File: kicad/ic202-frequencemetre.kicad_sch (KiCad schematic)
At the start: 40 parts, among them J1 +12V IN, J2 RF IN, J4 LCD, Q1 2N2369, U1 L7805, U2 LM317L, U3 MB506

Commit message: Documente l'intention de conception via la propriete Placement
Applique le skill conception-electronique-kicad au schema existant :
propriete masquee Placement posee sur chaque composant dont la position
finale importe au-dela du raccordement electrique.

Decouplage documente (prefixe LOCAL) : C1/C2 (entree J1, IN de U1), C3/C4
(noeud partage OUT U1 / VI U2), C5/C6 (sortie U2), C9 (VCC de U3), C8 (~IN
de U3, decouplage HF sur broche signal - pas une broche d'alimentation),
C11 (rail +3V pres de R6, point le plus eloigne du regulateur), C12
(reference VLCD_MID).

Verification systematique menee : les trois CI actifs (U1, U2, U3) ont
chacun leur decouplage local documente. A1 (module Arduino complet, deja
decouple en interne) volontairement hors de cette verification.

Boucles critiques documentees (prefixe LOOP CRITIQUE, hors decouplage) :
J2-R3-C7 (chemin RF d'entree vers U3, jusqu'a 2,4GHz), et
U3(OUT)-R19-C10-R4-R6-Q1 (chemin de comptage vers D5_SIG de A1, le signal
que l'instrument mesure).

Aucun changement electrique ni visuel : proprietes masquees par defaut,
netlist identique (40 composants, 22 nets), rendu confirme inchange. ERC :
0 erreur, 0 avertissement. Regles de lisibilite verifiees.

Co-Authored-By: Claude Sonnet 5 <noreply@anthropic.com>
Claude-Session: https://claude.ai/code/session_017jkpXZgM5sH1vt8JFfAijf
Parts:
- C1: Placement (none) -> LOCAL - decouplage HF, coller pres de l'entree J1 et de la 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
- C10: Placement (none) -> LOOP CRITIQUE - pas du decouplage : couplage AC + chemin de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
- C11: Placement (none) -> LOCAL - decouplage HF du rail +3V pres de R6 (tirage collec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
- C12: Placement (none) -> LOCAL - decouplage de la reference VLCD_MID, coller au poin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
- C2: Placement (none) -> LOCAL - decouplage bulk BF, coller pres de l'entree J1 et d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
- C3: Placement (none) -> LOCAL - decouplage HF, coller au noeud +5V (broche 3 OUT de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
- C4: Placement (none) -> LOCAL - decouplage bulk BF, coller au noeud +5V (broche 3 O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
- C5: Placement (none) -> LOCAL - decouplage HF, coller broche 2 (VO, sortie) de U2
- C6: Placement (none) -> LOCAL - decouplage bulk BF, coller broche 2 (VO, sortie) de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
- C7: Placement (none) -> LOOP CRITIQUE - pas du decouplage : couplage AC + chemin RF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
- C8: Placement (none) -> LOCAL - decouplage HF de la broche 8 (~IN, entree complemen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
- C9: Placement (none) -> LOCAL - decouplage HF, coller broche 2 (VCC) de U3
- J2, R3: Placement (none) -> LOOP CRITIQUE - chemin RF d'entree J2-R3-C7 vers U3 (broche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
- Q1, R4, R6: Placement (none) -> LOOP CRITIQUE - chemin de comptage U3(OUT)-R19-C10-R4-R6-Q1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
- R19: Placement (none) -> LOOP CRITIQUE - pas du decouplage : terminaison + chemin de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
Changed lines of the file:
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@@
 			)
 		)
+    (property "Placement" "LOCAL - decouplage HF, coller pres de l'entree J1 et de la broche 1 (IN) de U1" (at 48.26 38.1 0)
+      (effects (font (size 1.27 1.27)) (hide yes))
+    )
 		(pin "1"
 		)
@@
 			)
 		)
+    (property "Placement" "LOCAL - decouplage HF, coller au noeud +5V (broche 3 OUT de U1 / broche 3 VI de U2)" (at 104.14 38.1 0)
+      (effects (font (size 1.27 1.27)) (hide yes))
+    )
 		(pin "1"
 		)
@@
 			)
 		)
+    (property "Placement" "LOCAL - decouplage bulk BF, coller pres de l'entree J1 et de la broche 1 (IN) de U1" (at 58.42 38.1 0)
+      (effects (font (size 1.27 1.27)) (hide yes))
+    )
 		(pin "1"
 		)
@@
 			)
 		)
+    (property "Placement" "LOCAL - decouplage de la reference VLCD_MID, coller au point milieu du pont R17/R18" (at 309.88 220.98 0)
+      (effects (font (size 1.27 1.27)) (hide yes))
+    )
 		(pin "1"
 		)
@@
 			)
 		)
+    (property "Placement" "LOCAL - decouplage HF de la broche 8 (~IN, entree complementaire) de U3 vers la masse, pas du decouplage d'alimentation - coller a la broche avec R20" (at 55.88 114.3 0)
+      (effects (font (size 1.27 1.27)) (hide yes))
+    )
 		(pin "1"
 		)
@@
 			)
 		)
+    (property "Placement" "LOOP CRITIQUE - chemin de comptage U3(OUT)-R19-C10-R4-R6-Q1 vers D5_SIG (broche 8 de A1), surface minimale, eloigner des sources de bruit" (at 142.24 95.25 0)
+      (effects (font (size 1.27 1.27)) (hide yes))
+    )
 		(pin "1"
 		)
@@
 			)
 		)
+    (property "Placement" "LOOP CRITIQUE - pas du decouplage : terminaison + chemin de comptage U3(OUT)-R19-C10-R4-R6-Q1 vers D5_SIG (broche 8 de A1), surface minimale, eloigner des sources de bruit" (at 107.95 109.22 0)
+      (effects (font (size 1.27 1.27)) (hide yes))
+    )
 		(pin "1"
 		)
@@
 			)
 		)
+    (property "Placement" "LOCAL - decouplage HF du rail +3V pres de R6 (tirage collecteur Q1), point le plus eloigne du regulateur U2" (at 280.67 102.87 0)
+      (effects (font (size 1.27 1.27)) (hide yes))
+    )
 		(pin "1"
 		)
@@
 			)
 		)
+    (property "Placement" "LOCAL - decouplage bulk BF, coller au noeud +5V (broche 3 OUT de U1 / broche 3 VI de U2)" (at 114.3 38.1 0)
+      (effects (font (size 1.27 1.27)) (hide yes))
+    )
 		(pin "1"
 		)
@@
 			)
 		)
+    (property "Placement" "LOCAL - decouplage bulk BF, coller broche 2 (VO, sortie) de U2" (at 193.04 38.1 0)
+      (effects (font (size 1.27 1.27)) (hide yes))
+    )
 		(pin "1"
 		)
@@
 			)
 		)
+    (property "Placement" "LOOP CRITIQUE - pas du decouplage : couplage AC + chemin RF d'entree J2-R3-C7 vers U3 (broche 1, IN), surface minimale imperative (signal jusqu'a 2,4GHz)" (at 60.96 101.6 0)
+      (effects (font (size 1.27 1.27)) (hide yes))
+    )
 		(pin "1"
 		)
@@
 			)
 		)
+    (property "Placement" "LOOP CRITIQUE - chemin de comptage U3(OUT)-R19-C10-R4-R6-Q1 vers D5_SIG (broche 8 de A1), surface minimale, eloigner des sources de bruit" (at 162.56 86.36 0)
+      (effects (font (size 1.27 1.27)) (hide yes))
+    )
 		(pin "1"
 		)
@@
 			)
 		)
+    (property "Placement" "LOOP CRITIQUE - chemin de comptage U3(OUT)-R19-C10-R4-R6-Q1 vers D5_SIG (broche 8 de A1), surface minimale, eloigner des sources de bruit" (at 160.02 101.6 0)
+      (effects (font (size 1.27 1.27)) (hide yes))
+    )
 		(pin "1"
 		)
@@
 			)
 		)
+    (property "Placement" "LOOP CRITIQUE - pas du decouplage : couplage AC + chemin de comptage U3(OUT)-R19-C10-R4-R6-Q1 vers D5_SIG (broche 8 de A1), surface minimale, eloigner des sources de bruit" (at 119.38 101.6 0)
+      (effects (font (size 1.27 1.27)) (hide yes))
+    )
 		(pin "1"
 		)
@@
 			)
 		)
+    (property "Placement" "LOCAL - decouplage HF, coller broche 2 (VO, sortie) de U2" (at 182.88 38.1 0)
+      (effects (font (size 1.27 1.27)) (hide yes))
+    )
 		(pin "1"
 		)
@@
 			)
 		)
+    (property "Placement" "LOOP CRITIQUE - chemin RF d'entree J2-R3-C7 vers U3 (broche 1, IN), surface minimale imperative (signal jusqu'a 2,4GHz)" (at 43.18 109.22 0)
+      (effects (font (size 1.27 1.27)) (hide yes))
+    )
 		(pin "1"
 		)
@@
 			)
 		)
+    (property "Placement" "LOCAL - decouplage HF, coller broche 2 (VCC) de U3" (at 104.14 127.0 0)
+      (effects (font (size 1.27 1.27)) (hide yes))
+    )
 		(pin "1"
 		)
@@
 			)
 		)
-		(pin "1"
-		)
+    (property "Placement" "LOOP CRITIQUE - chemin RF d'entree J2-R3-C7 vers U3 (broche 1, IN), surface minimale imperative (signal jusqu'a 2,4GHz)" (at 30.48 101.6 0)
+      (effects (font (size 1.27 1.27)) (hide yes))
+    )
+		(pin "1"
+		)

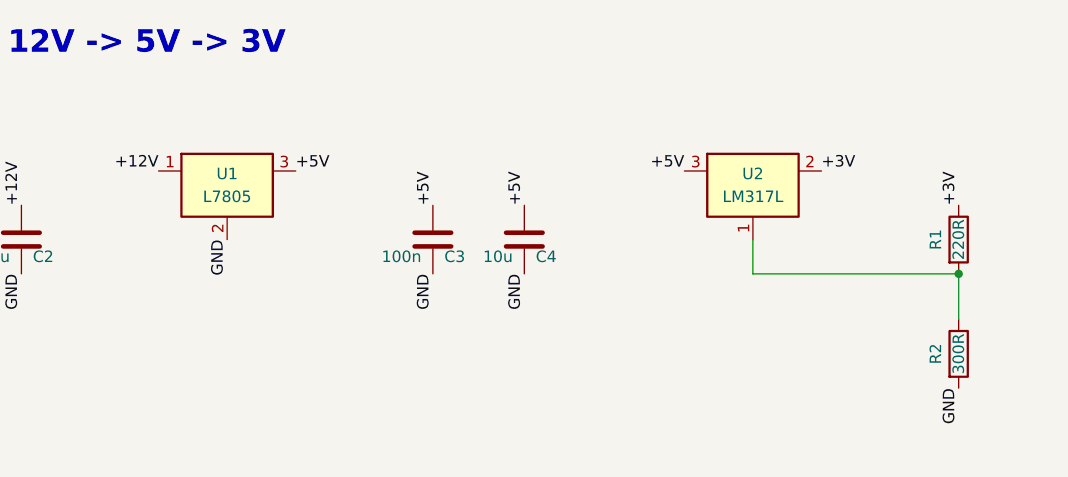
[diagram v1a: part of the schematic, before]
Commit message: Regulateurs en CMS : L7805->AMS1117-5.0, LM317L->AMS1117 ajustable
Stock PartsBox de l'utilisateur consulte avant de figer le choix (suivant
le skill conception-electronique-kicad) : ni L7805 ni LM317L en CMS en
stock, mais AMS1117-5.0 (68), AMS1117 ajustable (10) et AMS1117-3.3 (71)
en SOT-223, tous chez le meme fournisseur de stockage (C3 small
regulators). Choix retenu par l'utilisateur : AMS1117-5.0 pour U1,
AMS1117 ajustable pour U2 - topologie inchangee (meme reference 1,25V que
le LM317, R1/R2 conserves a l'identique).

Geometrie de broches verifiee avant remplacement : AMS1117-5.0 et L7805
partagent les memes coordonnees de broches (seule la numerotation change :
IN/OUT deviennent VI=broche3/VO=broche2), AMS1117 ajustable et LM317L_TO92
partagent numerotation ET coordonnees a l'identique. replace_schematic_
component utilise pour preserver position/rotation ; connectivite
reverifiee par export netlist apres coup - correcte des le premier essai.

Empreinte SOT-223-3_TabPin2 pour les deux (tab electriquement relie a VO,
conforme au brochage reel de l'AMS1117), rechargement pcbnew confirme.

Proprietes Placement de C1-C4 mises a jour pour refleter la nouvelle
numerotation des broches de U1. README revu integralement (alimentation,
mise en forme, tableau d'hypotheses, tableau de decouplage).

ERC : 0 erreur, 0 avertissement. Netlist identique (40 composants, 22
nets). Regles de lisibilite verifiees.

Co-Authored-By: Claude Sonnet 5 <noreply@anthropic.com>
Claude-Session: https://claude.ai/code/session_017jkpXZgM5sH1vt8JFfAijf
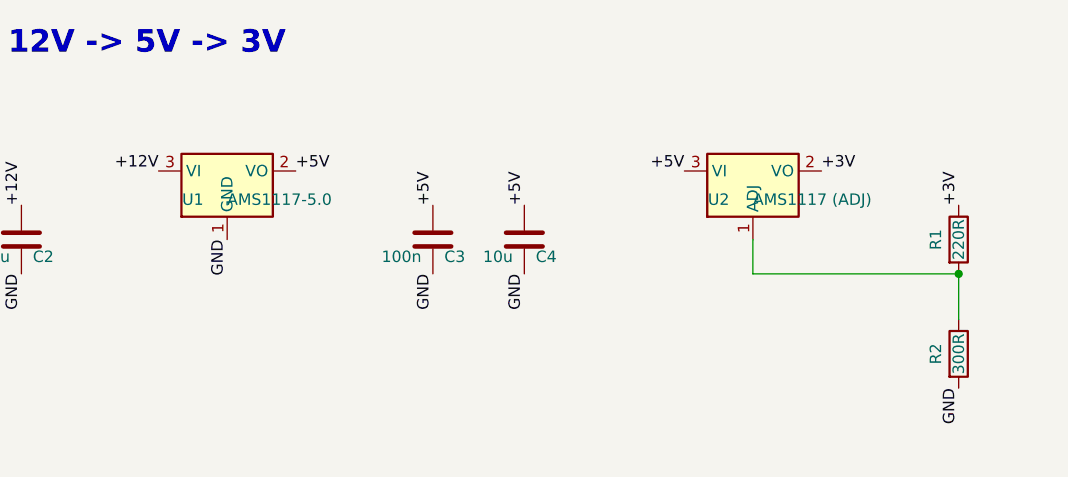
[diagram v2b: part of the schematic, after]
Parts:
- removed U1: L7805, Package_TO_SOT_THT:TO-220-3_Vertical, symbol Regulator_Linear:L7805
- removed U2: LM317L, Package_TO_SOT_THT:TO-92_Inline, symbol Regulator_Linear:LM317L_TO92
- added U1: AMS1117-5.0, Package_TO_SOT_SMD:SOT-223-3_TabPin2, symbol Regulator_Linear:AMS1117-5.0
- added U2: AMS1117 (ADJ), Package_TO_SOT_SMD:SOT-223-3_TabPin2, symbol Regulator_Linear:AMS1117
- C1: Placement LOCAL - decouplage HF, coller pres de l'entree J1 et de la broche 1 (IN) de U1 -> LOCAL - decouplage HF, coller pres de l'entree J1 et de la broche 3 (VI) de U1
- C2: Placement LOCAL - decouplage bulk BF, coller pres de l'entree J1 et de la broche 1 (IN) de U1 -> LOCAL - decouplage bulk BF, coller pres de l'entree J1 et de la broche 3 (VI) de U1
- C3: Placement LOCAL - decouplage HF, coller au noeud +5V (broche 3 OUT de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 -> LOCAL - decouplage HF, coller au noeud +5V (broche 2 VO de 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
- C4: Placement LOCAL - decouplage bulk BF, coller au noeud +5V (broche 3 O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 -> LOCAL - decouplage bulk BF, coller au noeud +5V (broche 2 V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
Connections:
- net +12V: now also U1.3 (VI)
- net +3V: now also U2.2 (VO)
- net +5V: now also U1.2 (VO), U2.3 (VI)
- net GND: now also U1.1 (GND)
- net at R1.2, R2.1: now also U2.1 (ADJ)

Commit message: U3->SOP-8, Q1->SOT-89, J1->4 broches ; cavaliers devant J4 ; replacement 80x50mm
Schema :
- U3 (MB506) : DIP-8 -> SOP-8 (MB506PF Fujitsu, stock PartsBox), meme
  brochage 1-8, pas de changement de symbole.
- Q1 : 2N2369 (TO-18) -> 2SC5551AE-TD-E (onsemi, SOT-89, fT=3.5GHz, stock
  PartsBox). Symbole remplace par Q_NPN_BCE (meme geometrie de broches que
  Q_NPN_BEC, seul l'etiquetage broche/fonction change) pour correspondre au
  brochage reel du SOT-89 (broche 2 = collecteur sur la languette).
- J1 : connecteur 2 broches -> 4 broches, paires adjacentes 1-2=+12V et
  3-4=GND. Corrige au passage un bug preexistant (les 2 broches d'origine
  et leurs labels +12V/GND etaient orphelins, non relies par un fil).
- 10 cavaliers a souder JP1-JP10 (Jumper:SolderJumper_2_Open, ouverts par
  defaut) inseres en serie entre R7-R16 et chaque broche de J4, pour
  pouvoir isoler la carte de la nappe LCD.

PCB :
- Board reduit de 80x70mm a 80x50mm.
- Nouveau placement complet : A1 decale de 3mm vers la gauche, R7-R16
  places dans le volume libre sous A1 (entre les deux barrettes de picots),
  reste reparti par proximite. 0 erreur run_drc (kicad-cli), 3
  avertissements silkscreen cosmetiques.
- Limitation d'outil documentee (README + skill kicad-pcb-placement) :
  check_courtyard_overlaps (MCP) juge sur la bounding box globale d'une
  empreinte, pas ses polygones reels - faux positifs sur les empreintes a
  courtyards multiples comme celle de A1. run_drc fait foi.

Co-Authored-By: Claude Sonnet 5 <noreply@anthropic.com>
Claude-Session: https://claude.ai/code/session_017jkpXZgM5sH1vt8JFfAijf
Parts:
- removed J1: +12V IN, Connector_PinHeader_2.54mm:PinHeader_1x02_P2.54mm_Vertical, symbol Connector_Generic:Conn_01x02
- removed Q1: 2N2369, Package_TO_SOT_THT:TO-92_Inline, symbol Transistor_BJT:Q_NPN_BEC
- added J1: +12V IN (4 pins: 2x+12V, 2x GND), Connector_PinHeader_2.54mm:PinHeader_1x04_P2.54mm_Vertical, symbol Connector_Generic:Conn_01x04
- added JP1, JP10, JP2, JP3, JP4, JP5, JP6, JP7, JP8, JP9: SolderJumper_2_Open, Jumper:SolderJumper-2_P1.3mm_Open_Pad1.0x1.5mm, symbol Jumper:SolderJumper_2_Open
- added Q1: 2SC5551AE-TD-E, Package_TO_SOT_SMD:SOT-89-3, symbol Transistor_BJT:Q_NPN_BCE
- U3: footprint Package_DIP:DIP-8_W7.62mm -> Package_SO:SOIC-8_5.3x6.2mm_P1.27mm
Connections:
- net +12V: now also J1.1 (Pin_1), J1.2 (Pin_2)
- net D5_SIG: now also Q1.2 (C)
- net GND: now also J1.3 (Pin_3), J1.4 (Pin_4), Q1.3 (E)
- net LCD_COM1: now also JP1.1 (A); no longer J4.1 (Pin_1)
- net LCD_COM2: now also JP2.1 (A); no longer J4.2 (Pin_2)
- net LCD_COM3: now also JP3.1 (A); no longer J4.3 (Pin_3)
- net LCD_COM4: now also JP4.1 (A); no longer J4.4 (Pin_4)
- net LCD_SEG1: now also JP5.1 (A); no longer J4.5 (Pin_5)
- net LCD_SEG2: now also JP6.1 (A); no longer J4.6 (Pin_6)
- net LCD_SEG3: now also JP7.1 (A); no longer J4.7 (Pin_7)
- net LCD_SEG4: now also JP8.1 (A); no longer J4.8 (Pin_8)
- net LCD_SEG5: now also JP9.1 (A); no longer J4.9 (Pin_9)
- net LCD_SEG6: now also JP10.1 (A); no longer J4.10 (Pin_10)
- net at C10.2, R4.1: now also Q1.1 (B)
- new net: J4.10 (Pin_10), J4.7 (Pin_7), J4.8 (Pin_8), J4.9 (Pin_9), JP10.2 (B), JP7.2 (B), JP8.2 (B), JP9.2 (B)
- new net: J4.1 (Pin_1), J4.2 (Pin_2), J4.3 (Pin_3), J4.4 (Pin_4), J4.5 (Pin_5), JP1.2 (B), JP2.2 (B), JP3.2 (B), JP4.2 (B), JP5.2 (B)
- new net: J4.6 (Pin_6), JP6.2 (B)

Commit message: Corrige un court-circuit entre lignes LCD introduit par le routage des cavaliers
Les 10 fils cavalier->J4 passaient par un coude a abscisse commune
(x=330.2). Les pas differents cote resistances (5,08mm) et cote J4
(2,54mm) faisaient que plusieurs segments verticaux se chevauchaient sur
cette abscisse, court-circuitant COM2-COM3-COM4-SEG1 d'un cote et
SEG3-SEG4 de l'autre. Trouve en tentant un premier routage (l'ERC ne
signalait qu'un avertissement discret, pas une erreur).

Corrige : les 10 chemins coudes remplaces par un fil diagonal unique par
ligne (aucun point partage entre lignes differentes). Chaque broche de J4
recoit aussi un label explicite (J4_COM1..J4_SEG6) : sync_schematic_to_board
echouait silencieusement a resoudre les nets anonymes auto-generes par
KiCad, laissant ces broches sans net cote PCB.

Verifie via kicad-cli sch export netlist (parse par comptage de
parentheses, pas de grep naif) : chaque ligne LCD forme maintenant
exactement 2 nets distincts et corrects. ERC : 0 erreur (3 avertissements
label_multiple_wires cosmetiques). run_drc PCB : 0 erreur.

Pieges documentes dans le skill kicad (nets anonymes non resolus par
sync_schematic_to_board, chevauchement de coudes de routage a pas
differents, necessite de parser le netlist par comptage de parentheses).

Co-Authored-By: Claude Sonnet 5 <noreply@anthropic.com>
Claude-Session: https://claude.ai/code/session_017jkpXZgM5sH1vt8JFfAijf
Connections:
- net J4_SEG2: now reaches J4.6 (Pin_6), JP6.2 (B)
- new net J4_COM1: J4.1 (Pin_1), JP1.2 (B)
- new net J4_COM2: J4.2 (Pin_2), JP2.2 (B)
- new net J4_COM3: J4.3 (Pin_3), JP3.2 (B)
- new net J4_COM4: J4.4 (Pin_4), JP4.2 (B)
- new net J4_SEG1: J4.5 (Pin_5), JP5.2 (B)
- new net J4_SEG3: J4.7 (Pin_7), JP7.2 (B)
- new net J4_SEG4: J4.8 (Pin_8), JP8.2 (B)
- new net J4_SEG5: J4.9 (Pin_9), JP9.2 (B)
- new net J4_SEG6: J4.10 (Pin_10), JP10.2 (B)

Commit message: Corrige 5 broches actives sans net (bug critique non detecte par ERC/DRC)
Trouve via inspection visuelle : la broche 1 de U3 semblait connectee a
trop d'endroits. Cause reelle : 5 nets sans label explicite (Net-(U3-IN),
Net-(U3-OUT), Net-(U3-~{IN}), Net-(Q1-B), Net-(U2-ADJ)) - valides au
schema, ERC silencieux - mais que sync_schematic_to_board echoue a
resoudre, laissant ces broches sans net du tout cote PCB. Consequence
reelle : la sortie du prescaler U3 et la base de Q1 n'ont jamais ete
reliees a la chaine de comptage, sur aucune des deux cartes, malgre un DRC
a 0 erreur (une broche sans net n'a aucune obligation de clearance envers
les autres nets).

Corrige :
- 5 nets renommes explicitement (MB506_IN, MB506_OUT, MB506_NIN, Q1_BASE,
  U2_ADJ), verifie via kicad-cli sch export netlist (parse par comptage de
  parentheses) qu'aucun net actif ne reste anonyme.
- Regle de clearance globale du board remontee de 0mm a 0.2mm (masquait
  d'autres risques de contact accidentel sur toute la carte, pas
  seulement a U3).
- Carte principale entierement reroutee (327 pistes, 40 vias) apres
  resynchronisation : 0 erreur run_drc.

Nouvelle regle ajoutee au skill conception-electronique-kicad : verifier
via kicad-cli sch export netlist qu'aucune broche active de composant ne
repose sur un net anonyme (Net-(...)) avant tout premier routage.

Co-Authored-By: Claude Sonnet 5 <noreply@anthropic.com>
Claude-Session: https://claude.ai/code/session_017jkpXZgM5sH1vt8JFfAijf
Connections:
- net U2_ADJ: now reaches R1.2, R2.1, U2.1 (ADJ)
- net MB506_NIN: now reaches C8.1, R20.1, U3.8 (~{IN})
- net Q1_BASE: now reaches C10.2, Q1.1 (B), R4.1
- net MB506_OUT: now reaches C10.1, R19.1, U3.4 (OUT)
- net MB506_IN: now reaches C7.2, U3.1 (IN)
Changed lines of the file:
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@@
+		)
+	)
+	(label "MB506_IN"
+		(at 73.66 101.60000000000001 0)
+		(effects
+			(font
+				(size 1.27 1.27)
+			)
+			(justify left bottom)
+		)
+	)
+	(label "MB506_OUT"
+		(at 99.06 101.60000000000001 180)
+		(effects
+			(font
+				(size 1.27 1.27)
+			)
+			(justify right bottom)
+		)
+	)
+	(label "MB506_NIN"
+		(at 73.66 104.14 0)
+		(effects
+			(font
+				(size 1.27 1.27)
+			)
+			(justify left bottom)
+		)
+	)
+	(label "Q1_BASE"
+		(at 154.94 101.6 0)
+		(effects
+			(font
+				(size 1.27 1.27)
+			)
+			(justify left bottom)
+		)
+	)
+	(label "U2_ADJ"
+		(at 139.7 38.1 90)
+		(effects
+			(font
+				(size 1.27 1.27)
+			)
+			(justify left bottom)
 		)
 	)

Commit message: Cavaliers a souder fermes par defaut ; supprime le PCB a rerouter
JP1..JP10 (coupure des lignes LCD devant J4) passent de l'empreinte
SolderJumper-2_P1.3mm_Open a la variante Bridged, et du symbole
Jumper:SolderJumper_2_Open a Jumper:SolderJumper_2_Bridged : la liaison
vers la nappe LCD est donc normale a la livraison, et c'est la coupure au
cutter qui devient l'action volontaire.

Autour du MB506, SW1 (broche 3) et SW2 (broche 6) ne sont plus reliees
directement au +5 V : elles y arrivent a travers JP11 et JP12, deux
cavaliers fermes, sur les nouveaux nets MB506_SW1 et MB506_SW2. Fermes,
les deux broches restent au niveau H et la division reste 1/64, donc le
fonctionnement est inchange ; couper un cavalier remet la broche en l'air
(niveau L) et donne 1/128, couper les deux donne 1/256.

La broche 7 ne recoit pas de cavalier : la datasheet Fujitsu la donne NC,
le rapport de division est fixe par SW1 et SW2 seulement. Elle garde son
no_connect.

Verifications : ERC identique a l'avant-modification (3 avertissements
label_multiple_wires preexistants, 0 erreur) ; comparaison des netlists
avant/apres : les 42 autres nets sont inchanges, les seules differences
sont l'ajout de JP11/JP12, le retrait de U3.3/U3.6 du net +5V et les deux
nouveaux nets de selection.

Le .kicad_pcb est supprime : le schema ayant deux composants de plus, le
placement et le routage seront refaits de zero avec de nouvelles
directives. Il reste recuperable via git show 34aeb82:kicad/ic202-frequencemetre.kicad_pcb

Co-Authored-By: Claude Opus 5 <noreply@anthropic.com>
Claude-Session: https://claude.ai/code/session_01RhWrMpVReTKTmWSsKndnB3
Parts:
- added JP11, JP12: SolderJumper_2_Bridged, Jumper:SolderJumper-2_P1.3mm_Bridged_Pad1.0x1.5mm, symbol Jumper:SolderJumper_2_Bridged
- JP1, JP10, JP2, JP3, JP4, JP5, JP6, JP7, JP8, JP9: value SolderJumper_2_Open -> SolderJumper_2_Bridged; footprint Jumper:SolderJumper-2_P1.3mm_Open_Pad1.0x1.5mm -> Jumper:SolderJumper-2_P1.3mm_Bridged_Pad1.0x1.5mm; symbol Jumper:SolderJumper_2_Open -> Jumper:SolderJumper_2_Bridged
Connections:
- net +5V: now also JP11.2 (B), JP12.2 (B); no longer U3.3 (SW1), U3.6 (SW2)
- new net MB506_SW1: JP11.1 (A), U3.3 (SW1)
- new net MB506_SW2: JP12.1 (A), U3.6 (SW2)
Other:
- note added: "PREDIVISEUR MB506 (division 1/64 par defaut, JP11/JP12)"
- note added: "R7..R16 : polarisation a mi-tension. Broche Arduino en haute impedance = 1,5 V, sinon 0 ou 3 V. JP1..JP10 : cavaliers fermes par defaut ; les couper isole la carte de la nappe LCD."
- note added: "SW1 (JP11) et SW2 (JP12) relies a +5V (niveau H) par cavaliers fermes : division par 64. Couper un cavalier = broche en l'air (niveau L) : 1/128 ; couper les deux : 1/256. Voir README."
- note removed: "PREDIVISEUR MB506 (division fixe 1/64)"
- note removed: "R7..R16 : polarisation a mi-tension. Broche Arduino en haute impedance = 1,5 V, sinon 0 ou 3 V."
- note removed: "SW1 et SW2 relies a +5V (niveau H) : division fixe par 64. Voir README."
